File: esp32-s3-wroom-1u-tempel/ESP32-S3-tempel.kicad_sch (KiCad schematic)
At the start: 33 parts, among them J1 USB, J2 USB2UART, J3 West, J4 East, J5 Nort, J6 South, Q1 SS8050, Q2 SS8050, SW1 RST, SW2 Boot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

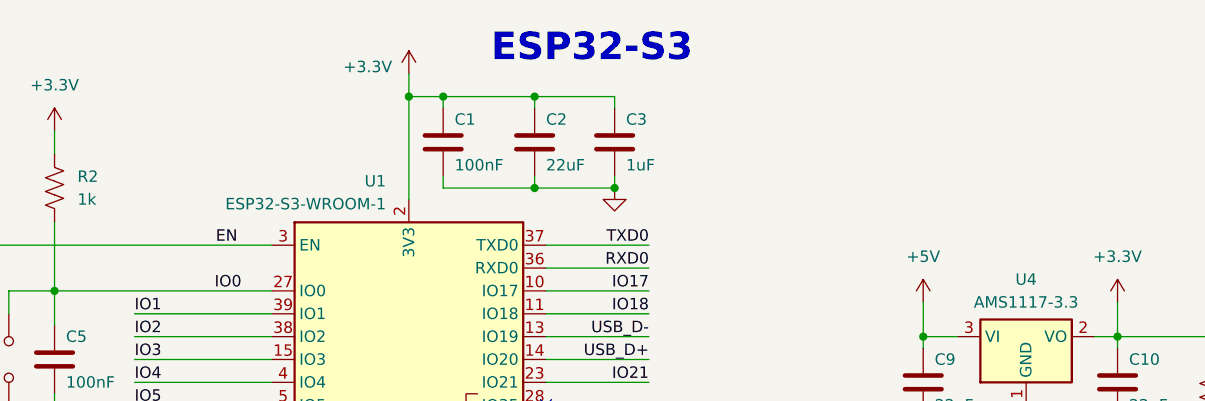
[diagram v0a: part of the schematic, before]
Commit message: feat: duplicate wroom 1u to wroom 1 (built in antenas)
n
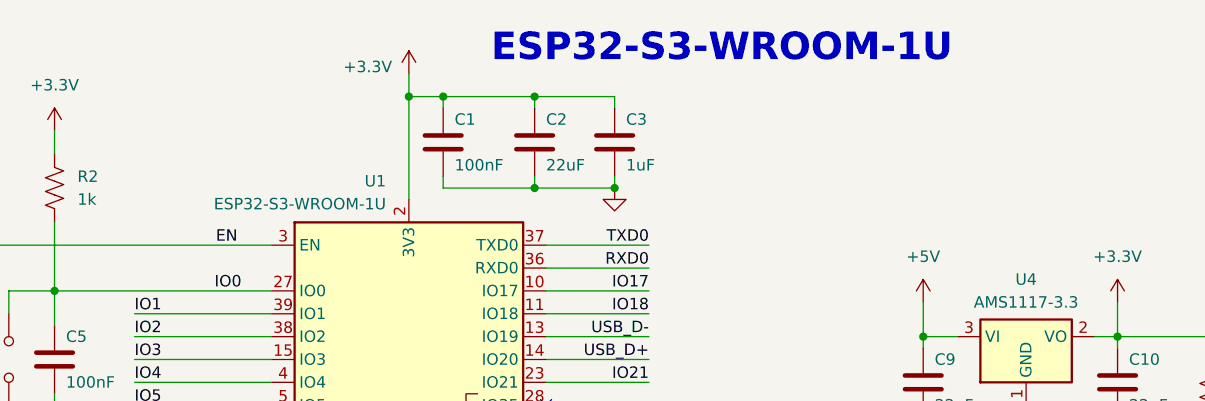
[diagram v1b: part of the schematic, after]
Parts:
- U1: value ESP32-S3-WROOM-1 -> ESP32-S3-WROOM-1U
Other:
- note added: "ESP32-S3-WROOM-1U"
- note removed: "ESP32-S3"
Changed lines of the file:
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@@
 		)
 	)
-	(text "ESP32-S3"
+	(text "ESP32-S3-WROOM-1U"
 		(exclude_from_sim no)
 		(at 98.044 15.748 0)
@@
 			)
 		)
-		(property "Value" "ESP32-S3-WROOM-1"
+		(property "Value" "ESP32-S3-WROOM-1U"
 			(at 86.36 34.798 0)
 			(effects
